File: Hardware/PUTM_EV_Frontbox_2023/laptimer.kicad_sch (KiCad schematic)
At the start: 0 parts

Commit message: Schematic ready for review
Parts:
- added R68: 1k, symbol Device:R_Small
- added U11: TLP291-4, Package_SO:SOIC-16_4.55x10.3mm_P1.27mm, symbol Isolator:TLP291-4
- added U17: TSOP21xx, OptoDevice:Vishay_MOLD-3Pin, symbol Interface_Optical:TSOP21xx
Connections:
- net Laptimer_in: now also R68.1, U17.1 (OUT)
- net Laptimer_out: now also U11.9
- new net: R68.2, U11.7
- new net +3.3V: U11.10
- new net +5V: U17.2 (Vs)
- new net GND: U11.8, U17.3 (GND)
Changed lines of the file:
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@@
   (title_block
     (title "Laptimer")
-    (date "2023-02-24")
+    (date "2023-03-11")
     (rev "${REVISION}")
     (company "Author: Szymon Kostrubiec")
     (comment 1 "Reviewer:")
   )
-  (hierarchical_label "Laptimer_in" (shape input) (at 142.24 88.9 0) (fields_autoplaced)
+  (wire (pts (xy 161.29 104.14) (xy 163.195 104.14))
+    (stroke (width 0) (type default))
+  )
+  (wire (pts (xy 125.095 113.03) (xy 125.095 111.76))
+    (stroke (width 0) (type default))
+  )
+  (wire (pts (xy 125.095 101.6) (xy 125.095 100.33))
+    (stroke (width 0) (type default))
+  )
+  (wire (pts (xy 125.095 111.76) (xy 123.825 111.76))
+    (stroke (width 0) (type default))
+  )
+  (wire (pts (xy 161.925 109.22) (xy 163.195 109.22))
+    (stroke (width 0) (type default))
+  )
+  (wire (pts (xy 154.305 104.14) (xy 156.21 104.14))
+    (stroke (width 0) (type default))
+  )
+  (wire (pts (xy 178.435 104.14) (xy 179.705 104.14))
+    (stroke (width 0) (type default))
+  )
+  (wire (pts (xy 179.705 104.14) (xy 179.705 102.87))
+    (stroke (width 0) (type default))
+  )
+  (wire (pts (xy 161.925 110.49) (xy 161.925 109.22))
+    (stroke (width 0) (type default))
+  )
+  (wire (pts (xy 123.825 101.6) (xy 125.095 101.6))
+    (stroke (width 0) (type default))
+  )
+  (hierarchical_label "Laptimer_in" (shape input) (at 154.305 104.14 180) (fields_autoplaced)
+    (effects (font (size 1.27 1.27)) (justify right))
+  )
+  (hierarchical_label "Laptimer_in" (shape input) (at 123.825 106.68 0) (fields_autoplaced)
     (effects (font (size 1.27 1.27)) (justify left))
   )
-  (hierarchical_label "Laptimer_out" (shape output) (at 163.83 88.265 0) (fields_autoplaced)
+  (hierarchical_label "Laptimer_out" (shape input) (at 178.435 109.22 0) (fields_autoplaced)
     (effects (font (size 1.27 1.27)) (justify left))
   )
+  (symbol (lib_id "Isolator:TLP291-4") (at 170.815 106.68 0) (unit 4)
+    (in_bom yes) (on_board yes) (dnp no) (fields_autoplaced)
+    (property "Reference" "U11" (at 170.815 99.06 0)
+      (effects (font (size 1.27 1.27)))
+    )
+    (property "Value" "TLP291-4" (at 170.815 101.6 0)
+      (effects (font (size 1.27 1.27)))
+    )
+    (property "Footprint" "Package_SO:SOIC-16_4.55x10.3mm_P1.27mm" (at 165.735 111.76 0)
+      (effects (font (size 1.27 1.27) italic) (justify left) hide)
+    )
+    (property "Datasheet" "https://toshiba.semicon-storage.com/info/docget.jsp?did=12858&prodName=TLP291-4" (at 170.815 106.68 0)
+      (effects (font (size 1.27 1.27)) (justify left) hide)
+    )
+    (pin "1")
+    (pin "15")
+    (pin "16")
+    (pin "2")
+    (pin "13")
+    (pin "14")
+    (pin "3")
+    (pin "4")
+    (pin "11")
+    (pin "12")
+    (pin "5")
+    (pin "6")
+    (pin "10")
+    (pin "7")
+    (pin "8")
+    (pin "9")
+    (instances
+      (project "PUTM_EV_Frontbox_2023"
+        (path "/b652b05a-4e3d-4ad1-b032-18886abe7d45/d8521410-c497-472e-ae31-9f909ba7779b"
+          (reference "U11") (unit 4)
+        )
+        (path "/b652b05a-4e3d-4ad1-b032-18886abe7d45/a8c4f732-a122-416e-8a5e-65ca70330696"
+          (reference "U11") (unit 4)
+        )
+      )
+    )
+  )
+  (symbol (lib_id "power:+5V") (at 125.095 100.33 0) (unit 1)
+    (in_bom yes) (on_board yes) (dnp no) (fields_autoplaced)
+    (property "Reference" "#PWR0116" (at 125.095 104.14 0)
+      (effects (font (size 1.27 1.27)) hide)
+    )
+    (property "Value" "+5V" (at 125.095 96.52 0)
+      (effects (font (size 1.27 1.27)))
+    )
+    (property "Footprint" "" (at 125.095 100.33 0)
+      (effects (font (size 1.27 1.27)) hide)
+    )
+    (property "Datasheet" "" (at 125.095 100.33 0)
+      (effects (font (size 1.27 1.27)) hide)
+    )
+    (pin "1")
+    (instances
+      (project "PUTM_EV_Frontbox_2023"
+        (path "/b652b05a-4e3d-4ad1-b032-18886abe7d45/a8c4f732-a122-416e-8a5e-65ca70330696"
+          (reference "#PWR0116") (unit 1)
+        )
+      )
+    )
+  )
+  (symbol (lib_id "power:+3.3V") (at 179.705 102.87 0) (unit 1)
+    (in_bom yes) (on_board yes) (dnp no) (fields_autoplaced)
+    (property "Reference" "#PWR0119" (at 179.705 106.68 0)
+      (effects (font (size 1.27 1.27)) hide)
+    )
+    (property "Value" "+3.3V" (at 179.705 99.06 0)
+      (effects (font (size 1.27 1.27)))
+    )
+    (property "Footprint" "" (at 179.705 102.87 0)
+      (effects (font (size 1.27 1.27)) hide)
+    )
+    (property "Datasheet" "" (at 179.705 102.87 0)
+      (effects (font (size 1.27 1.27)) hide)
+    )
+    (pin "1")
+    (instances
+      (project "PUTM_EV_Frontbox_2023"
+        (path "/b652b05a-4e3d-4ad1-b032-18886abe7d45/a8c4f732-a122-416e-8a5e-65ca70330696"
+          (reference "#PWR0119") (unit 1)
+        )
+      )
+    )
+  )
+  (symbol (lib_id "power:GND") (at 125.095 113.03 0) (unit 1)
+    (in_bom yes) (on_board yes) (dnp no)
+    (property "Reference" "#PWR0117" (at 125.095 119.38 0)
+      (effects (font (size 1.27 1.27)) hide)
+    )
+    (property "Value" "GND" (at 125.095 116.84 0)
+      (effects (font (size 1.27 1.27)))
+    )
+    (property "Footprint" "" (at 125.095 113.03 0)
+      (effects (font (size 1.27 1.27)) hide)
+    )
+    (property "Datasheet" "" (at 125.095 113.03 0)
+      (effects (font (size 1.27 1.27)) hide)
+    )
+    (pin "1")
+    (instances
+      (project "PUTM_EV_Frontbox_2023"
+        (path "/b652b05a-4e3d-4ad1-b032-18886abe7d45/a8c4f732-a122-416e-8a5e-65ca70330696"
+          (reference "#PWR0117") (unit 1)
+        )
+      )
+    )
+  )
+  (symbol (lib_id "power:GND") (at 161.925 110.49 0) (unit 1)
+    (in_bom yes) (on_board yes) (dnp no)
+    (property "Reference" "#PWR0118" (at 161.925 116.84 0)
+      (effects (font (size 1.27 1.27)) hide)
+    )
+    (property "Value" "GND" (at 161.925 114.3 0)
+      (effects (font (size 1.27 1.27)))
+    )
+    (property "Footprint" "" (at 161.925 110.49 0)
+      (effects (font (size 1.27 1.27)) hide)
+    )
+    (property "Datasheet" "" (at 161.925 110.49 0)
+      (effects (font (size 1.27 1.27)) hide)
+    )
+    (pin "1")
+    (instances
+      (project "PUTM_EV_Frontbox_2023"
+        (path "/b652b05a-4e3d-4ad1-b032-18886abe7d45/a8c4f732-a122-416e-8a5e-65ca70330696"
+          (reference "#PWR0118") (unit 1)
+        )
+      )
+    )
+  )
+  (symbol (lib_id "Device:R_Small") (at 158.75 104.14 90) (unit 1)
+    (in_bom yes) (on_board yes) (dnp no) (fields_autoplaced)
+    (property "Reference" "R68" (at 158.75 99.06 90)
+      (effects (font (size 1.27 1.27)))
+    )
+    (property "Value" "1k" (at 158.75 101.6 90)
+      (effects (font (size 1.27 1.27)))
+    )
+    (property "Footprint" "" (at 158.75 104.14 0)
+      (effects (font (size 1.27 1.27)) hide)
+    )
+    (property "Datasheet" "~" (at 158.75 104.14 0)
+      (effects (font (size 1.27 1.27)) hide)
+    )
+    (pin "1")
+    (pin "2")
+    (instances
+      (project "PUTM_EV_Frontbox_2023"
+        (path "/b652b05a-4e3d-4ad1-b032-18886abe7d45/d8521410-c497-472e-ae31-9f909ba7779b"
+          (reference "R68") (unit 1)
+        )
+        (path "/b652b05a-4e3d-4ad1-b032-18886abe7d45/a8c4f732-a122-416e-8a5e-65ca70330696"
+          (reference "R66") (unit 1)
+        )
+      )
+    )
+  )
+  (symbol (lib_id "Interface_Optical:TSOP21xx") (at 113.665 106.68 0) (unit 1)
+    (in_bom yes) (on_board yes) (dnp no) (fields_autoplaced)
+    (property "Reference" "U17" (at 111.93 95.885 0)
+      (effects (font (size 1.27 1.27)))
+    )
+    (property "Value" "TSOP21xx" (at 111.93 98.425 0)
+      (effects (font (size 1.27 1.27)))
+    )
+    (property "Footprint" "OptoDevice:Vishay_MOLD-3Pin" (at 112.395 116.205 0)
+      (effects (font (size 1.27 1.27)) hide)
+    )
+    (property "Datasheet" "http://www.vishay.com/docs/82460/tsop45.pdf" (at 130.175 99.06 0)
+      (effects (font (size 1.27 1.27)) hide)
+    )
+    (pin "1")
+    (pin "2")
+    (pin "3")
+    (instances
+      (project "PUTM_EV_Frontbox_2023"
+        (path "/b652b05a-4e3d-4ad1-b032-18886abe7d45/a8c4f732-a122-416e-8a5e-65ca70330696"
+          (reference "U17") (unit 1)
+        )
+      )
+    )
+  )
 )

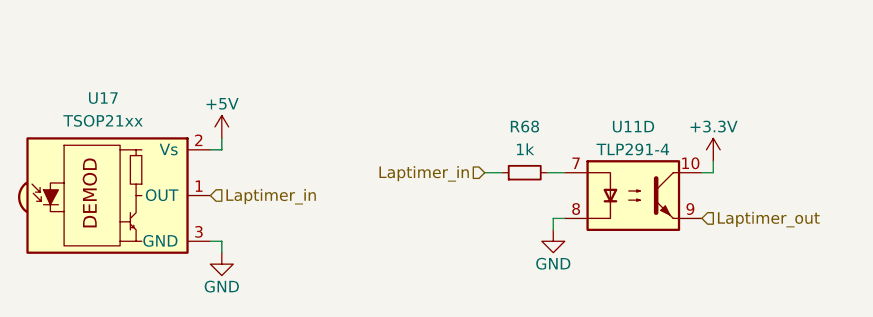
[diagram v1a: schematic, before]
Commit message: Added missing laptimer resistor
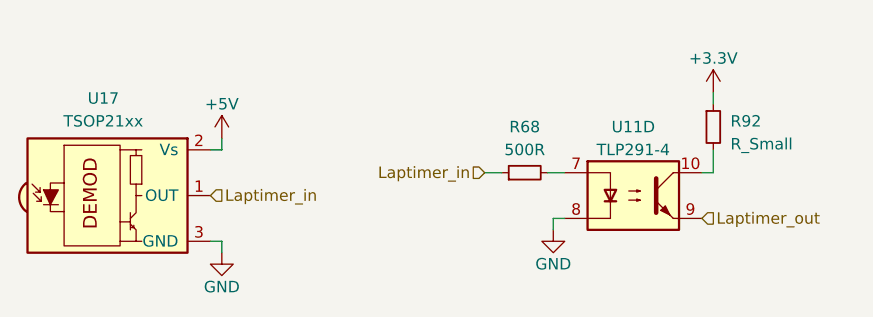
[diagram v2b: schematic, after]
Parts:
- added R92: R_Small, symbol Device:R_Small
- R68: value 1k -> 500R
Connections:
- net +3.3V: now also R92.1; no longer U11.10
- new net: R92.2, U11.10
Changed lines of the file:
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@@
     (stroke (width 0) (type default))
   )
-  (wire (pts (xy 179.705 104.14) (xy 179.705 102.87))
+  (wire (pts (xy 179.705 95.25) (xy 179.705 96.52))
+    (stroke (width 0) (type default))
+  )
+  (wire (pts (xy 179.705 101.6) (xy 179.705 104.14))
     (stroke (width 0) (type default))
   )
@@
     )
   )
+  (symbol (lib_id "Device:R_Small") (at 179.705 99.06 0) (unit 1)
+    (in_bom yes) (on_board yes) (dnp no) (fields_autoplaced)
+    (property "Reference" "R92" (at 181.61 98.425 0)
+      (effects (font (size 1.27 1.27)) (justify left))
+    )
+    (property "Value" "R_Small" (at 181.61 100.965 0)
+      (effects (font (size 1.27 1.27)) (justify left))
+    )
+    (property "Footprint" "" (at 179.705 99.06 0)
+      (effects (font (size 1.27 1.27)) hide)
+    )
+    (property "Datasheet" "~" (at 179.705 99.06 0)
+      (effects (font (size 1.27 1.27)) hide)
+    )
+    (pin "1")
+    (pin "2")
+    (instances
+      (project "PUTM_EV_Frontbox_2023"
+        (path "/b652b05a-4e3d-4ad1-b032-18886abe7d45/a8c4f732-a122-416e-8a5e-65ca70330696"
+          (reference "R92") (unit 1)
+        )
+      )
+    )
+  )
   (symbol (lib_id "power:+5V") (at 125.095 100.33 0) (unit 1)
     (in_bom yes) (on_board yes) (dnp no) (fields_autoplaced)
@@
     )
   )
-  (symbol (lib_id "power:+3.3V") (at 179.705 102.87 0) (unit 1)
+  (symbol (lib_id "power:+3.3V") (at 179.705 95.25 0) (unit 1)
     (in_bom yes) (on_board yes) (dnp no) (fields_autoplaced)
-    (property "Reference" "#PWR0119" (at 179.705 106.68 0)
+    (property "Reference" "#PWR0119" (at 179.705 99.06 0)
       (effects (font (size 1.27 1.27)) hide)
     )
-    (property "Value" "+3.3V" (at 179.705 99.06 0)
+    (property "Value" "+3.3V" (at 179.705 91.44 0)
       (effects (font (size 1.27 1.27)))
     )
-    (property "Footprint" "" (at 179.705 102.87 0)
+    (property "Footprint" "" (at 179.705 95.25 0)
       (effects (font (size 1.27 1.27)) hide)
     )
-    (property "Datasheet" "" (at 179.705 102.87 0)
+    (property "Datasheet" "" (at 179.705 95.25 0)
       (effects (font (size 1.27 1.27)) hide)
     )
@@
       (effects (font (size 1.27 1.27)))
     )
-    (property "Value" "1k" (at 158.75 101.6 90)
+    (property "Value" "500R" (at 158.75 101.6 90)
       (effects (font (size 1.27 1.27)))
     )

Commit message: Schematic modified, footprints assigned
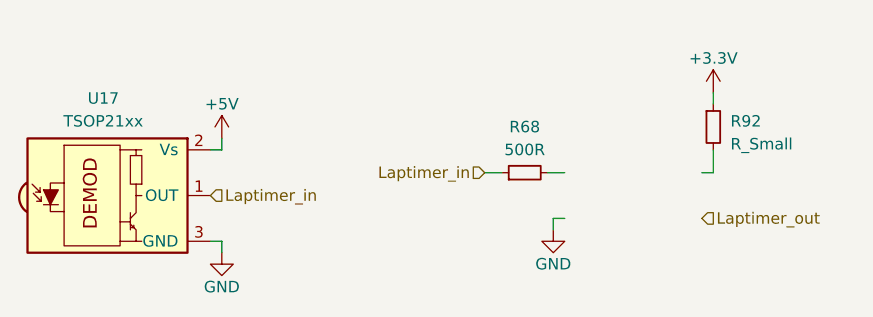
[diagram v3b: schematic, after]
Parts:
- removed U11: TLP291-4, Package_SO:SOIC-16_4.55x10.3mm_P1.27mm, symbol Isolator:TLP291-4
- R68, R92: footprint (none) -> Resistor_SMD:R_0603_1608Metric
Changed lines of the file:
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@@
     (effects (font (size 1.27 1.27)) (justify left))
-  )
-  (symbol (lib_id "Isolator:TLP291-4") (at 170.815 106.68 0) (unit 4)
-    (in_bom yes) (on_board yes) (dnp no) (fields_autoplaced)
-    (property "Reference" "U11" (at 170.815 99.06 0)
-      (effects (font (size 1.27 1.27)))
-    )
-    (property "Value" "TLP291-4" (at 170.815 101.6 0)
-      (effects (font (size 1.27 1.27)))
-    )
-    (property "Footprint" "Package_SO:SOIC-16_4.55x10.3mm_P1.27mm" (at 165.735 111.76 0)
-      (effects (font (size 1.27 1.27) italic) (justify left) hide)
-    )
-    (property "Datasheet" "https://toshiba.semicon-storage.com/info/docget.jsp?did=12858&prodName=TLP291-4" (at 170.815 106.68 0)
-      (effects (font (size 1.27 1.27)) (justify left) hide)
-    )
-    (pin "1")
-    (pin "15")
-    (pin "16")
-    (pin "2")
-    (pin "13")
-    (pin "14")
-    (pin "3")
-    (pin "4")
-    (pin "11")
-    (pin "12")
-    (pin "5")
-    (pin "6")
-    (pin "10")
-    (pin "7")
-    (pin "8")
-    (pin "9")
-    (instances
-      (project "PUTM_EV_Frontbox_2023"
-        (path "/b652b05a-4e3d-4ad1-b032-18886abe7d45/d8521410-c497-472e-ae31-9f909ba7779b"
-          (reference "U11") (unit 4)
-        )
-        (path "/b652b05a-4e3d-4ad1-b032-18886abe7d45/a8c4f732-a122-416e-8a5e-65ca70330696"
-          (reference "U11") (unit 4)
-        )
-      )
-    )
   )
   (symbol (lib_id "Device:R_Small") (at 179.705 99.06 0) (unit 1)
@@
       (effects (font (size 1.27 1.27)) (justify left))
     )
-    (property "Footprint" "" (at 179.705 99.06 0)
+    (property "Footprint" "Resistor_SMD:R_0603_1608Metric" (at 179.705 99.06 0)
       (effects (font (size 1.27 1.27)) hide)
     )
@@
       (effects (font (size 1.27 1.27)))
     )
-    (property "Footprint" "" (at 158.75 104.14 0)
+    (property "Footprint" "Resistor_SMD:R_0603_1608Metric" (at 158.75 104.14 0)
       (effects (font (size 1.27 1.27)) hide)
     )
